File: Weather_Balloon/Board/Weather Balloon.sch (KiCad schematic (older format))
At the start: 58 parts, among them IC1 ATTINY85-P, IC2 ATMEGA2560-A, P1 85_PRGM, P10 SERIAL, P2 ADC_AUX, P22 RADIO, P4 2560_RESET, P5 2560_SCK, P6 2560_MOSI, P7 2560_MISO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

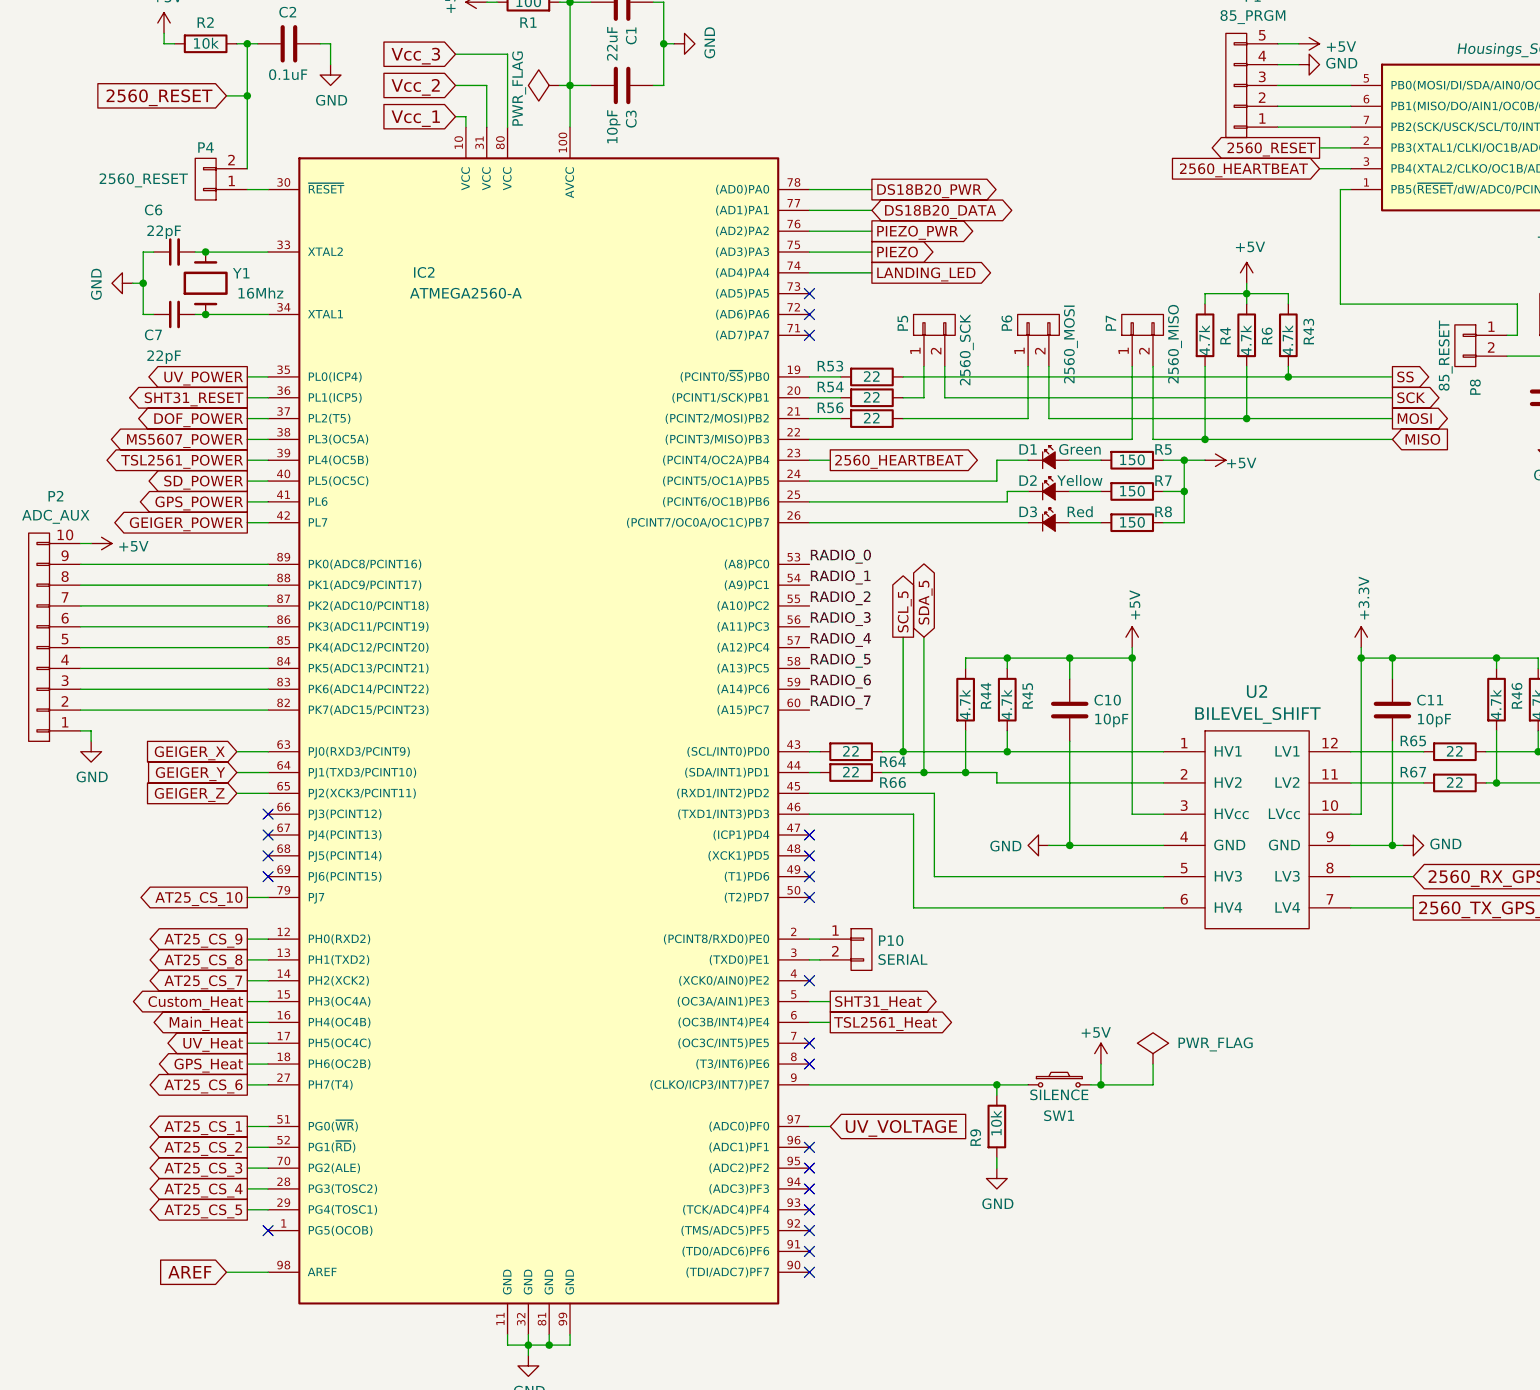
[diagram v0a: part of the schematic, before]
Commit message: Updated PCB board for larger traces and more compact design.
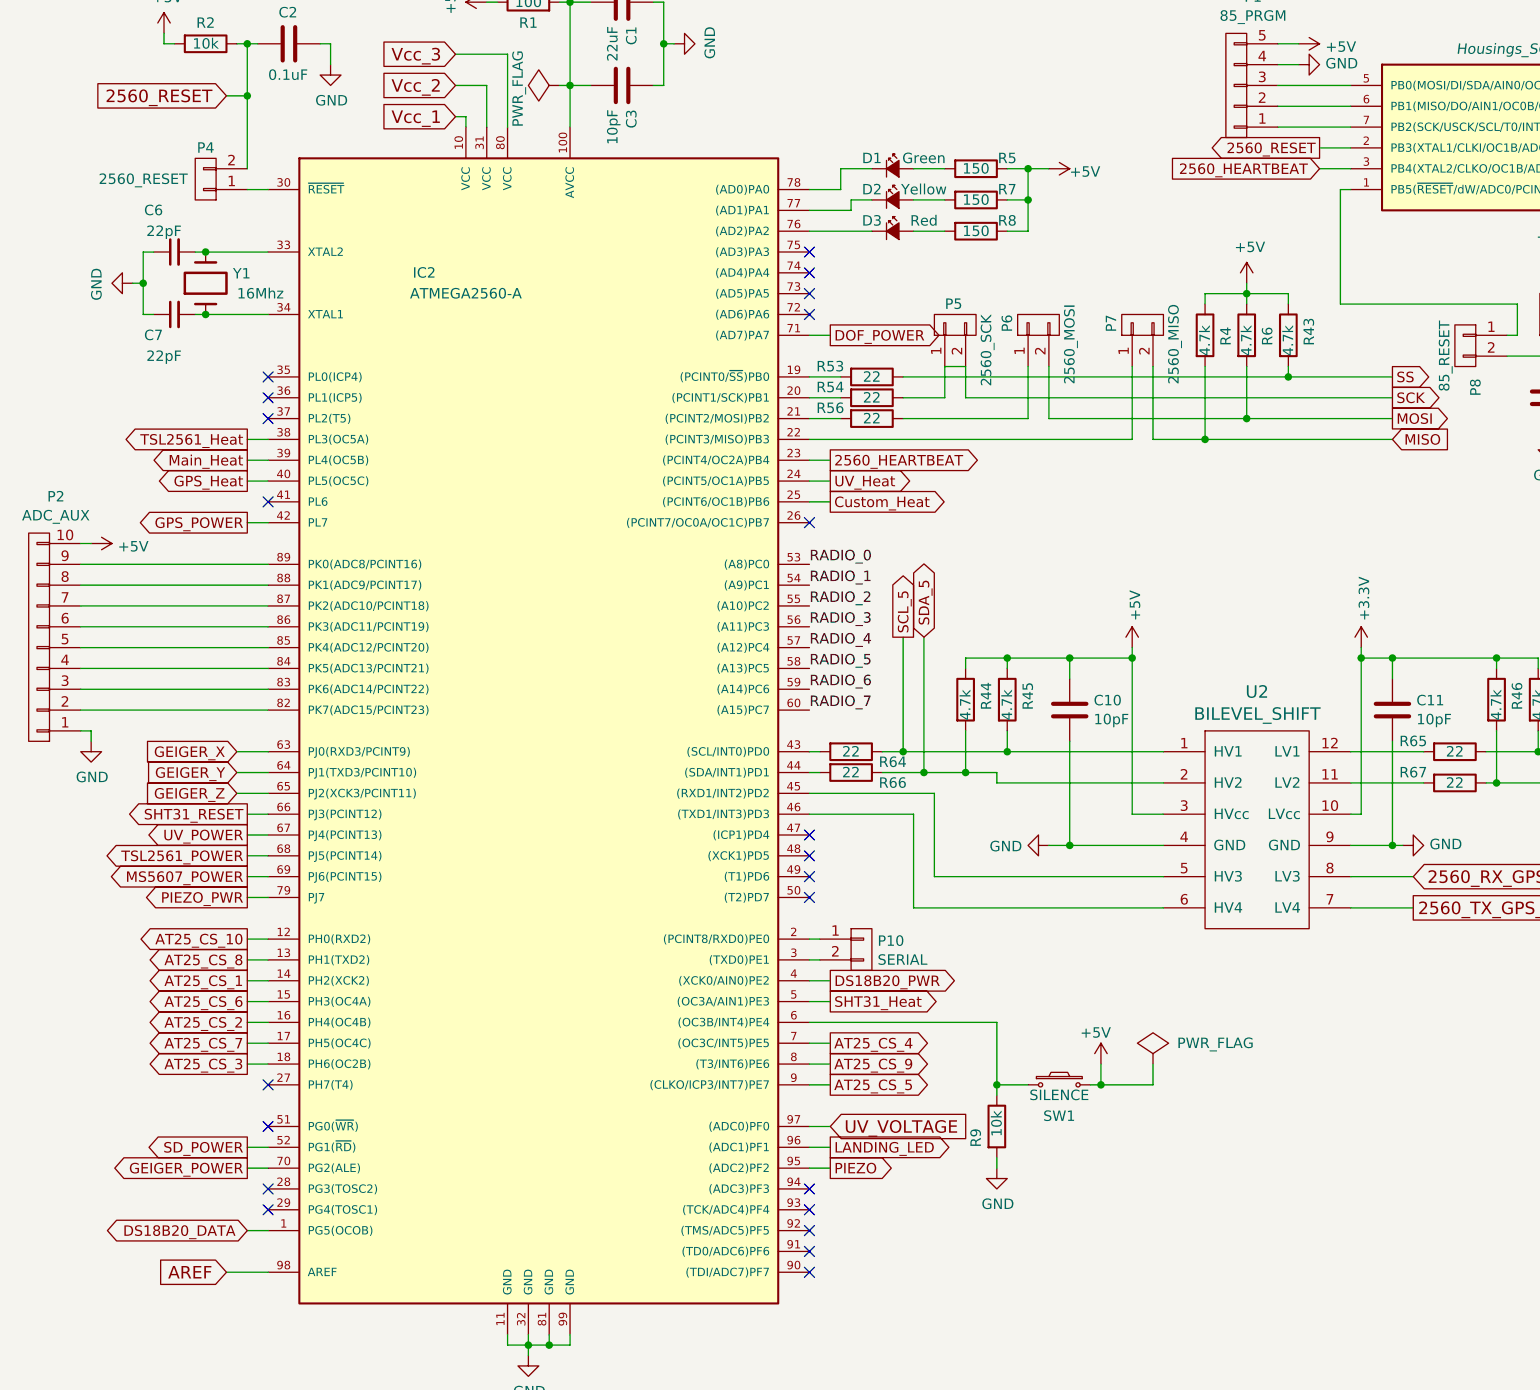
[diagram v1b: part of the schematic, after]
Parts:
- Y1: footprint Personal:HC-49V -> Crystals:HC-49V
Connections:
- net AT25_CS_1: now also IC2.14 (PH2(XCK2)); no longer IC2.51 (PG0(~WR~))
- net AT25_CS_10: now also IC2.12 (PH0(RXD2)); no longer IC2.79 (PJ7)
- net AT25_CS_2: now also IC2.16 (PH4(OC4B)); no longer IC2.52 (PG1(~RD~))
- net AT25_CS_3: now also IC2.18 (PH6(OC2B)); no longer IC2.70 (PG2(ALE))
- net AT25_CS_4: now also IC2.7 ((OC3C/INT5)PE5); no longer IC2.28 (PG3(TOSC2))
- net AT25_CS_5: now also IC2.9 ((CLKO/ICP3/INT7)PE7); no longer IC2.29 (PG4(TOSC1))
- net AT25_CS_6: now also IC2.15 (PH3(OC4A)); no longer IC2.27 (PH7(T4))
- net AT25_CS_7: now also IC2.17 (PH5(OC4C)); no longer IC2.14 (PH2(XCK2))
- net AT25_CS_9: now also IC2.8 ((T3/INT6)PE6); no longer IC2.12 (PH0(RXD2))
- net Custom_Heat: now also IC2.25 ((PCINT6/OC1B)PB6); no longer IC2.15 (PH3(OC4A))
- net DOF_POWER: now also IC2.71 ((AD7)PA7); no longer IC2.37 (PL2(T5))
- net DS18B20_DATA: now also IC2.1 (PG5(OCOB)); no longer IC2.77 ((AD1)PA1)
- net DS18B20_PWR: now also IC2.4 ((XCK0/AIN0)PE2); no longer IC2.78 ((AD0)PA0)
- net GEIGER_POWER: now also IC2.70 (PG2(ALE)); no longer IC2.42 (PL7)
- net GPS_Heat: now also IC2.40 (PL5(OC5C)); no longer IC2.18 (PH6(OC2B))
- net GPS_POWER: now also IC2.42 (PL7); no longer IC2.41 (PL6)
- net LANDING_LED: now also IC2.96 ((ADC1)PF1); no longer IC2.74 ((AD4)PA4)
- net MS5607_POWER: now also IC2.69 (PJ6(PCINT15)); no longer IC2.38 (PL3(OC5A))
- net Main_Heat: now also IC2.39 (PL4(OC5B)); no longer IC2.16 (PH4(OC4B))
- net PIEZO: now also IC2.95 ((ADC2)PF2); no longer IC2.75 ((AD3)PA3)
- net PIEZO_PWR: now also IC2.79 (PJ7); no longer IC2.76 ((AD2)PA2)
- net SCK: now also P5.1 (P1), R54.1
- net SD_POWER: now also IC2.52 (PG1(~RD~)); no longer IC2.40 (PL5(OC5C))
- net SHT31_RESET: now also IC2.66 (PJ3(PCINT12)); no longer IC2.36 (PL1(ICP5))
- net TSL2561_Heat: now also IC2.38 (PL3(OC5A)); no longer IC2.6 ((OC3B/INT4)PE4)
- net TSL2561_POWER: now also IC2.68 (PJ5(PCINT14)); no longer IC2.39 (PL4(OC5B))
- net UV_Heat: now also IC2.24 ((PCINT5/OC1A)PB5); no longer IC2.17 (PH5(OC4C))
- net UV_POWER: now also IC2.67 (PJ4(PCINT13)); no longer IC2.35 (PL0(ICP4))
- net at D1.1 (K): now also IC2.78 ((AD0)PA0); no longer IC2.24 ((PCINT5/OC1A)PB5)
- net at D2.1 (K): now also IC2.77 ((AD1)PA1); no longer IC2.25 ((PCINT6/OC1B)PB6)
- net at IC2.26 ((PCINT7/OC0A/OC1C)PB7): no longer D3.1 (K)
- net at R9.1, SW1.1: now also IC2.6 ((OC3B/INT4)PE4); no longer IC2.9 ((CLKO/ICP3/INT7)PE7)
- new net: D3.1 (K), IC2.76 ((AD2)PA2)
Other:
- moved on the sheet: D1, D2, D3, P5, R5, R7, R8

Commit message: PID control and beginning of altitude alarm.
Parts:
- SW1: footprint Buttons_Switches_ThroughHole:SW_PUSH-12mm -> Buttons_Switches_ThroughHole:SW_PUSH_6mm
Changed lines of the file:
@@
 Sheet 1 4
 Title "HAB Control Unit"
-Date "2016-09-26"
-Rev "v0.6"
+Date "2016-10-03"
+Rev "v1.4"
 Comp "Robert Susmilch"
 Comment1 ""
@@
 F 0 "SW1" H 5650 5750 50  0000 C CNN
 F 1 "SILENCE" H 5650 5850 50  0000 C CNN
-F 2 "Buttons_Switches_ThroughHole:SW_PUSH-12mm" H 5650 6100 50  0001 C CNN
+F 2 "Buttons_Switches_ThroughHole:SW_PUSH_6mm" H 5650 6100 50  0001 C CNN
 F 3 "" H 5650 6100 50  0000 C CNN
 	1    5650 5900
